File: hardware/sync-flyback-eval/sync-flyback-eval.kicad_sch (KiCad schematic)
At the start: 82 parts, among them J1 RJ45_LED_Shielded, Q1 SiR422DP, Q2 Si7898DP, Q3 MMDT3906, T1 PoE_Transformer, T2 Pulse_Transformer, U1 TPS23754PWPR, U2 TCMT1107

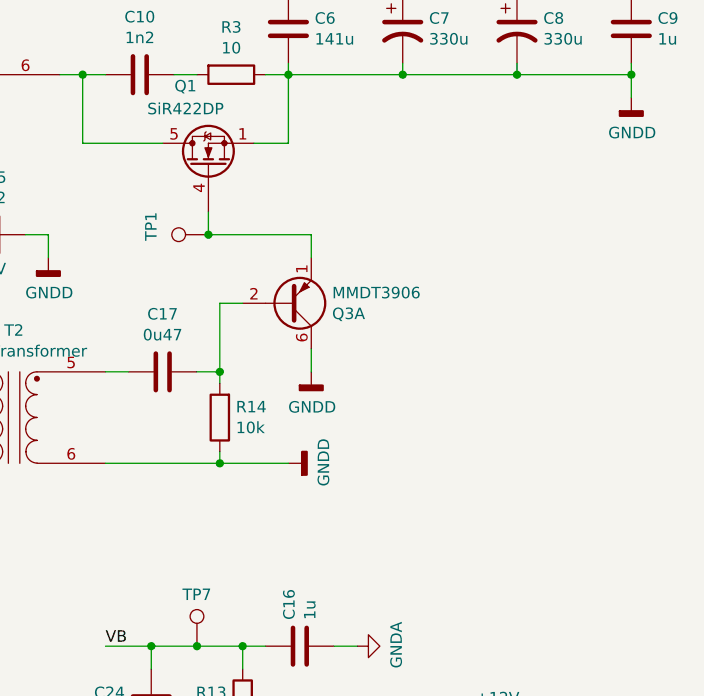
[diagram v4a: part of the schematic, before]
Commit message: flyback: add missing diode network across secondary-side gate
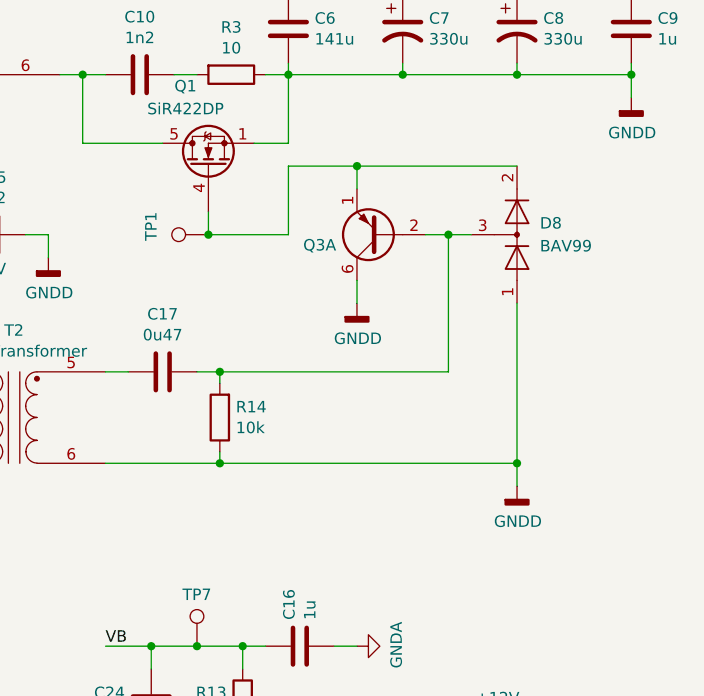
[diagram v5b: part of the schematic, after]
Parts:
- added D8: BAV99, Package_TO_SOT_SMD:SOT-23, symbol Diode:BAV99
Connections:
- net GNDD: now also D8.1 (K)
- net at C17.1, Q3.2 (B1), R14.2: now also D8.3 (K)
- net at Q1.4 (G), Q3.1 (E1), TP1.1: now also D8.2 (A)
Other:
- moved on the sheet: Q3A
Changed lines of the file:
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@@
   (junction (at 134.62 24.13) (diameter 0) (color 0 0 0 0)
   )
+  (junction (at 248.92 82.55) (diameter 0) (color 0 0 0 0)
+  )
   (junction (at 148.59 64.77) (diameter 0) (color 0 0 0 0)
   )
@@
   (junction (at 60.96 41.91) (diameter 0) (color 0 0 0 0)
   )
+  (junction (at 241.3 57.15) (diameter 0) (color 0 0 0 0)
+  )
   (junction (at 167.64 72.39) (diameter 0) (color 0 0 0 0)
   )
@@
   (junction (at 60.96 72.39) (diameter 0) (color 0 0 0 0)
   )
+  (junction (at 231.14 49.53) (diameter 0) (color 0 0 0 0)
+  )
   (junction (at 96.52 24.13) (diameter 0) (color 0 0 0 0)
   )
@@
     (stroke (width 0) (type default) (color 0 0 0 0))
   )
+  (wire (pts (xy 231.14 49.53) (xy 248.92 49.53))
+    (stroke (width 0) (type default) (color 0 0 0 0))
+  )
   (wire (pts (xy 138.43 54.61) (xy 138.43 57.15))
     (stroke (width 0) (type default) (color 0 0 0 0))
@@
     (stroke (width 0) (type default) (color 0 0 0 0))
   )
-  (wire (pts (xy 214.63 57.15) (xy 226.06 57.15))
+  (wire (pts (xy 214.63 57.15) (xy 223.52 57.15))
     (stroke (width 0) (type default) (color 0 0 0 0))
   )
@@
     (stroke (width 0) (type default) (color 0 0 0 0))
   )
+  (wire (pts (xy 231.14 49.53) (xy 231.14 52.07))
+    (stroke (width 0) (type default) (color 0 0 0 0))
+  )
   (wire (pts (xy 236.22 39.37) (xy 248.92 39.37))
     (stroke (width 0) (type default) (color 0 0 0 0))
@@
     (stroke (width 0) (type default) (color 0 0 0 0))
   )
-  (wire (pts (xy 226.06 72.39) (xy 226.06 69.85))
-    (stroke (width 0) (type default) (color 0 0 0 0))
-  )
   (wire (pts (xy 236.22 120.65) (xy 238.76 120.65))
     (stroke (width 0) (type default) (color 0 0 0 0))
@@
     (stroke (width 0) (type default) (color 0 0 0 0))
   )
-  (wire (pts (xy 226.06 57.15) (xy 226.06 59.69))
+  (wire (pts (xy 223.52 49.53) (xy 223.52 57.15))
     (stroke (width 0) (type default) (color 0 0 0 0))
   )
@@
     (stroke (width 0) (type default) (color 0 0 0 0))
   )
+  (wire (pts (xy 231.14 62.23) (xy 231.14 64.77))
+    (stroke (width 0) (type default) (color 0 0 0 0))
+  )
   (wire (pts (xy 182.88 82.55) (xy 182.88 96.52))
     (stroke (width 0) (type default) (color 0 0 0 0))
@@
     (stroke (width 0) (type default) (color 0 0 0 0))
   )
+  (wire (pts (xy 241.3 57.15) (xy 243.84 57.15))
+    (stroke (width 0) (type default) (color 0 0 0 0))
+  )
   (wire (pts (xy 35.56 57.15) (xy 35.56 67.31))
     (stroke (width 0) (type default) (color 0 0 0 0))
@@
     (stroke (width 0) (type default) (color 0 0 0 0))
   )
+  (wire (pts (xy 248.92 82.55) (xy 248.92 85.09))
+    (stroke (width 0) (type default) (color 0 0 0 0))
+  )
   (wire (pts (xy 111.76 167.64) (xy 114.3 167.64))
     (stroke (width 0) (type default) (color 0 0 0 0))
@@
     (stroke (width 0) (type default) (color 0 0 0 0))
   )
+  (wire (pts (xy 241.3 57.15) (xy 238.76 57.15))
+    (stroke (width 0) (type default) (color 0 0 0 0))
+  )
   (wire (pts (xy 261.62 29.21) (xy 261.62 30.48))
     (stroke (width 0) (type default) (color 0 0 0 0))
@@
     (stroke (width 0) (type default) (color 0 0 0 0))
   )
+  (wire (pts (xy 223.52 49.53) (xy 231.14 49.53))
+    (stroke (width 0) (type default) (color 0 0 0 0))
+  )
   (wire (pts (xy 132.08 77.47) (xy 132.08 80.01))
     (stroke (width 0) (type default) (color 0 0 0 0))
@@
     (stroke (width 0) (type default) (color 0 0 0 0))
   )
-  (wire (pts (xy 223.52 82.55) (xy 215.9 82.55))
+  (wire (pts (xy 215.9 82.55) (xy 248.92 82.55))
     (stroke (width 0) (type default) (color 0 0 0 0))
   )
@@
     (stroke (width 0) (type default) (color 0 0 0 0))
   )
+  (wire (pts (xy 241.3 72.39) (xy 241.3 57.15))
+    (stroke (width 0) (type default) (color 0 0 0 0))
+  )
   (wire (pts (xy 158.75 57.15) (xy 157.48 57.15))
     (stroke (width 0) (type default) (color 0 0 0 0))
@@
     (stroke (width 0) (type default) (color 0 0 0 0))
   )
-  (wire (pts (xy 215.9 72.39) (xy 215.9 64.77))
+  (wire (pts (xy 248.92 82.55) (xy 248.92 64.77))
     (stroke (width 0) (type default) (color 0 0 0 0))
   )
@@
     (stroke (width 0) (type default) (color 0 0 0 0))
   )
-  (wire (pts (xy 215.9 64.77) (xy 218.44 64.77))
+  (wire (pts (xy 215.9 72.39) (xy 241.3 72.39))
     (stroke (width 0) (type default) (color 0 0 0 0))
   )
@@
     (pin "2")
   )
-  (symbol (lib_id "Transistor_BJT:MMDT3906") (at 223.52 64.77 0) (mirror x) (unit 1)
+  (symbol (lib_id "Transistor_BJT:MMDT3906") (at 233.68 57.15 180) (unit 1)
     (in_bom yes) (on_board yes)
-    (property "Reference" "Q3" (id 0) (at 228.3714 65.9384 0)
+    (property "Reference" "Q3" (id 0) (at 228.8286 58.3184 0)
       (effects (font (size 1.27 1.27)) (justify left))
     )
-    (property "Value" "MMDT3906" (id 1) (at 228.3714 63.627 0)
-      (effects (font (size 1.27 1.27)) (justify left))
+    (property "Value" "MMDT3906" (id 1) (at 228.8286 56.007 0)
+      (effects (font (size 1.27 1.27)) (justify left) hide)
     )
-    (property "Footprint" "Package_TO_SOT_SMD:SOT-363_SC-70-6" (id 2) (at 228.6 67.31 0)
+    (property "Footprint" "Package_TO_SOT_SMD:SOT-363_SC-70-6" (id 2) (at 228.6 59.69 0)
       (effects (font (size 1.27 1.27)) hide)
     )
-    (property "Datasheet" "http://www.diodes.com/_files/datasheets/ds30124.pdf" (id 3) (at 223.52 64.77 0)
+    (property "Datasheet" "http://www.diodes.com/_files/datasheets/ds30124.pdf" (id 3) (at 233.68 57.15 0)
       (effects (font (size 1.27 1.27)) hide)
     )
@@
     (pin "1")
   )
-  (symbol (lib_id "power:GNDD") (at 223.52 82.55 90) (unit 1)
+  (symbol (lib_id "power:GNDD") (at 248.92 85.09 0) (unit 1)
     (in_bom yes) (on_board yes)
-    (property "Reference" "#PWR025" (id 0) (at 229.87 82.55 0)
+    (property "Reference" "#PWR025" (id 0) (at 248.92 91.44 0)
       (effects (font (size 1.27 1.27)) hide)
     )
-    (property "Value" "GNDD" (id 1) (at 227.457 82.4484 0))
-    (property "Footprint" "" (id 2) (at 223.52 82.55 0)
+    (property "Value" "GNDD" (id 1) (at 249.0216 89.027 0))
+    (property "Footprint" "" (id 2) (at 248.92 85.09 0)
       (effects (font (size 1.27 1.27)) hide)
     )
-    (property "Datasheet" "" (id 3) (at 223.52 82.55 0)
+    (property "Datasheet" "" (id 3) (at 248.92 85.09 0)
       (effects (font (size 1.27 1.27)) hide)
     )
@@
     (pin "1")
   )
-  (symbol (lib_id "power:GNDD") (at 226.06 72.39 0) (unit 1)
+  (symbol (lib_id "power:GNDD") (at 231.14 64.77 0) (unit 1)
     (in_bom yes) (on_board yes)
-    (property "Reference" "#PWR019" (id 0) (at 226.06 78.74 0)
+    (property "Reference" "#PWR019" (id 0) (at 231.14 71.12 0)
       (effects (font (size 1.27 1.27)) hide)
     )
-    (property "Value" "GNDD" (id 1) (at 226.1616 76.327 0))
-    (property "Footprint" "" (id 2) (at 226.06 72.39 0)
+    (property "Value" "GNDD" (id 1) (at 231.2416 68.707 0))
+    (property "Footprint" "" (id 2) (at 231.14 64.77 0)
       (effects (font (size 1.27 1.27)) hide)
     )
-    (property "Datasheet" "" (id 3) (at 226.06 72.39 0)
+    (property "Datasheet" "" (id 3) (at 231.14 64.77 0)
       (effects (font (size 1.27 1.27)) hide)
     )
@@
     (pin "1")
   )
+  (symbol (lib_id "Diode:BAV99") (at 248.92 57.15 270) (mirror x) (unit 1)
+    (in_bom yes) (on_board yes) (fields_autoplaced)
+    (property "Reference" "D8" (id 0) (at 251.46 55.8799 90)
+      (effects (font (size 1.27 1.27)) (justify left))
+    )
+    (property "Value" "BAV99" (id 1) (at 251.46 58.4199 90)
+      (effects (font (size 1.27 1.27)) (justify left))
+    )
+    (property "Footprint" "Package_TO_SOT_SMD:SOT-23" (id 2) (at 236.22 57.15 0)
+      (effects (font (size 1.27 1.27)) hide)
+    )
+    (property "Datasheet" "https://assets.nexperia.com/documents/data-sheet/BAV99_SER.pdf" (id 3) (at 248.92 57.15 0)
+      (effects (font (size 1.27 1.27)) hide)
+    )
+    (pin "1")
+    (pin "2")
+    (pin "3")
+  )
   (symbol (lib_id "Connector:TestPoint") (at 119.38 44.45 180) (unit 1)
     (in_bom yes) (on_board yes)
@@
       (reference "D7") (unit 1) (value "D") (footprint "Diode_SMD:D_SOD-323")
     )
+    (path "/cdfa2f3a-a0c9-4ac3-a482-27ce9ab24954"
+      (reference "D8") (unit 1) (value "BAV99") (footprint "Package_TO_SOT_SMD:SOT-23")
+    )
     (path "/00000000-0000-0000-0000-00005d56eab6"

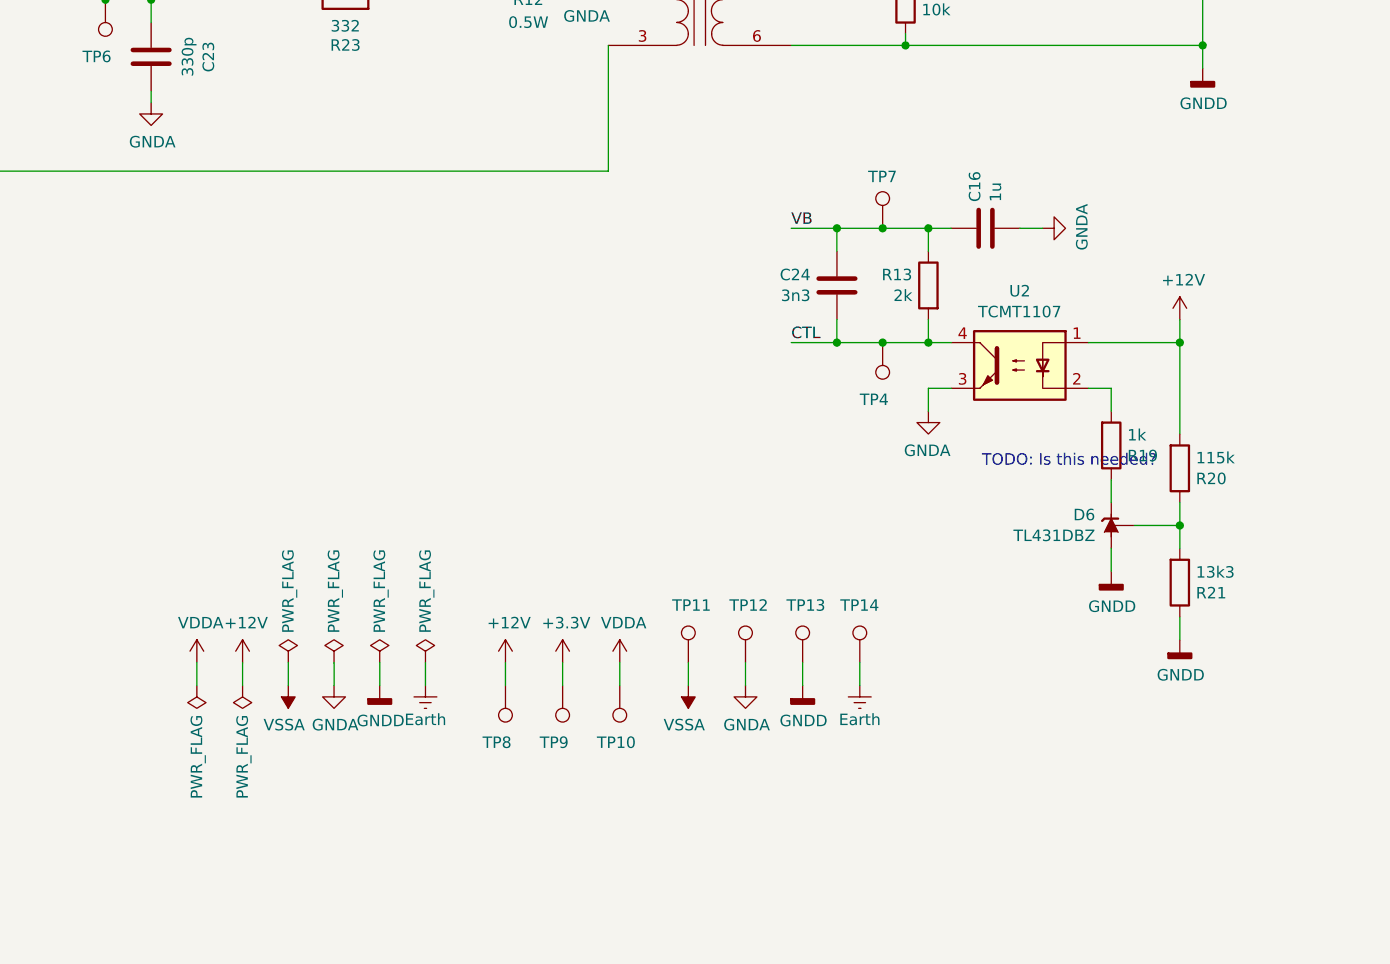
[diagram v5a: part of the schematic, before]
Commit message: flyback: add missing RC pair to primary-side sync feedback
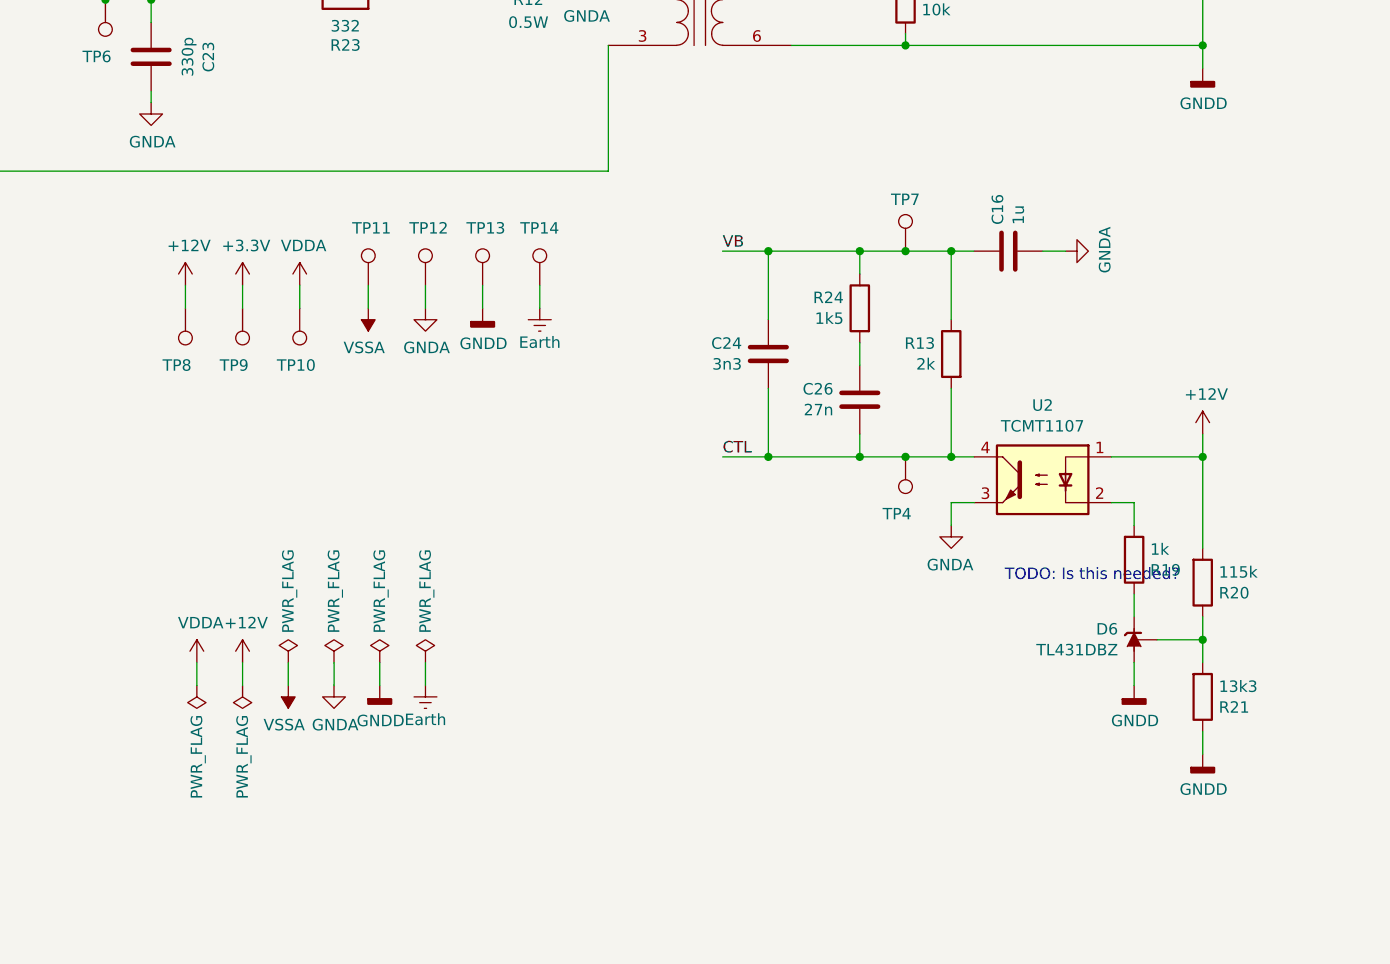
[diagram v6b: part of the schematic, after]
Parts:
- added C26: 27n, Capacitor_SMD:C_0402_1005Metric, symbol Device:C
- added R24: 1k5, Resistor_SMD:R_0402_1005Metric, symbol Device:R
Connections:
- net CTL: now also C26.2
- net VB: now also R24.1
- new net: C26.1, R24.2
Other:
- moved on the sheet: C16, C24, D6, R13, R19, R20, R21, TP10, TP11, TP12, TP13, TP14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

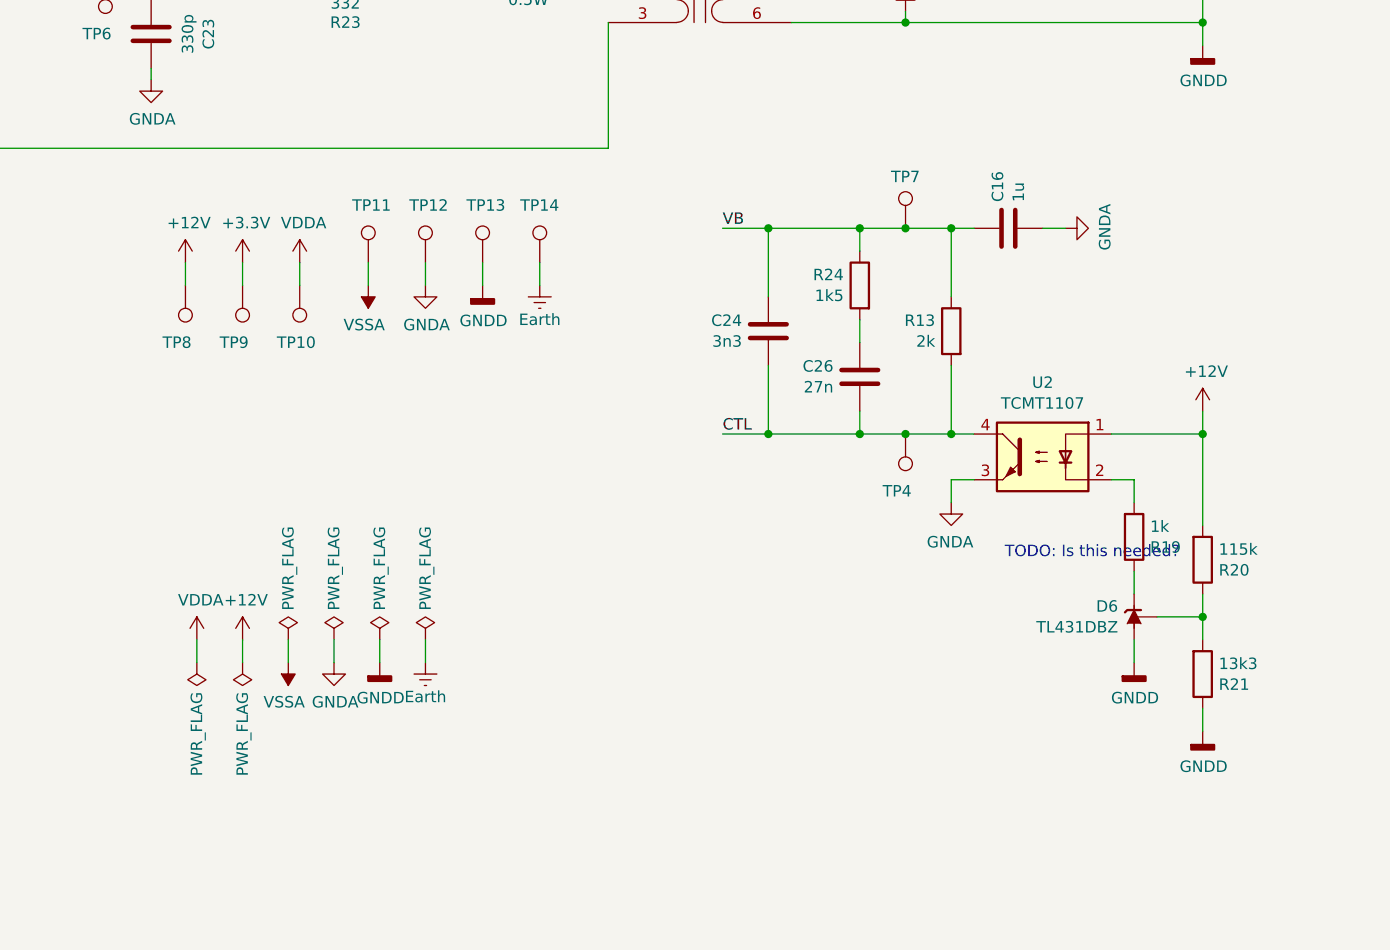
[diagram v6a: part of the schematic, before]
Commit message: flyback: build out secondary-side of synchronous feedback loop
This more-closely follows the application note, adapted for a 12-volt output.
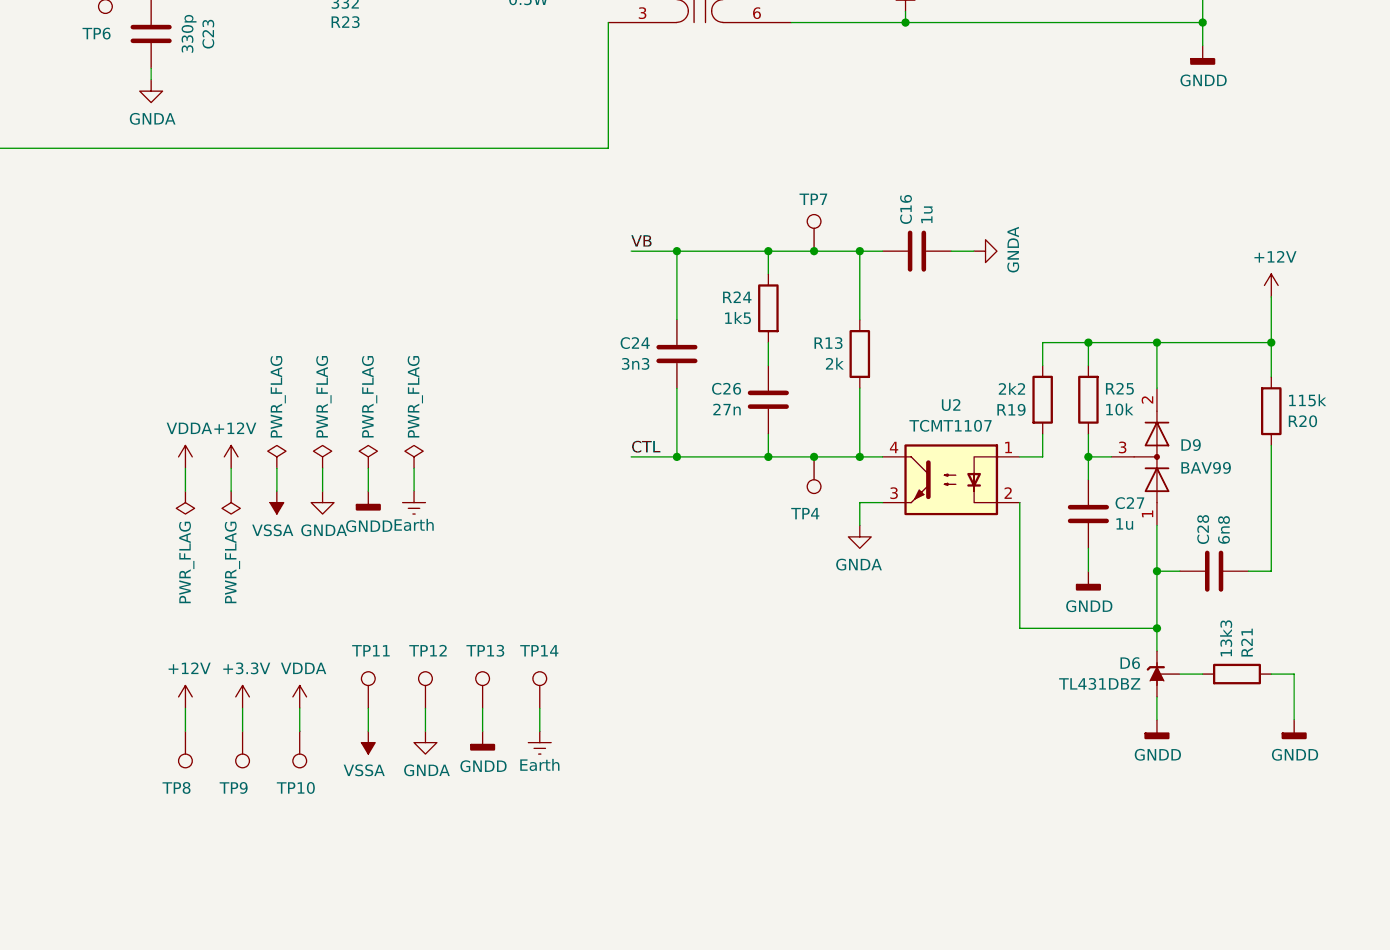
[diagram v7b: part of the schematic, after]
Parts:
- added C27: 1u, Capacitor_SMD:C_0402_1005Metric, symbol Device:C
- added C28: 6n8, Capacitor_SMD:C_0402_1005Metric, symbol Device:C
- added D9: BAV99, Package_TO_SOT_SMD:SOT-23, symbol Diode:BAV99
- added R25: 10k, Resistor_SMD:R_0402_1005Metric, symbol Device:R
- R19: value 1k -> 2k2
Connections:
- net +12V: now also R19.1, D9.2 (A), R25.2; no longer U2.1
- net GNDD: now also C27.2
- net at R19.2: now also U2.1; no longer U2.2
- net at D6.1 (K): now also U2.2, C28.1, D9.1 (K); no longer R19.1
- net at D6.2 (REF), R21.2: no longer R20.1
- new net: C28.2, R20.1
- new net: C27.1, D9.3 (K), R25.1
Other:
- note removed: "TODO: Is this needed?"
- moved on the sheet: C16, C24, C26, D6, R13, R20, R21, R24, TP10, TP11, TP12, TP13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
